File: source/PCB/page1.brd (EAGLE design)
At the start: 74.9 x 45.5 mm, 22 parts, among them J1 MJ88-BX11-RVSL2, J2 CONNECTOR-HEADER-6P-3460650P1, J4 CONNECTOR-HEADER-3P-3460810P1, J5 CONNECTOR-HEADER-2X3P-3460180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, Q3 MOSFET-N-044020001, Q4 MOSFET-N-044020001, U1 ATMEGA328P-AU-1030060P1, U2 A4988SETTR-QFN28

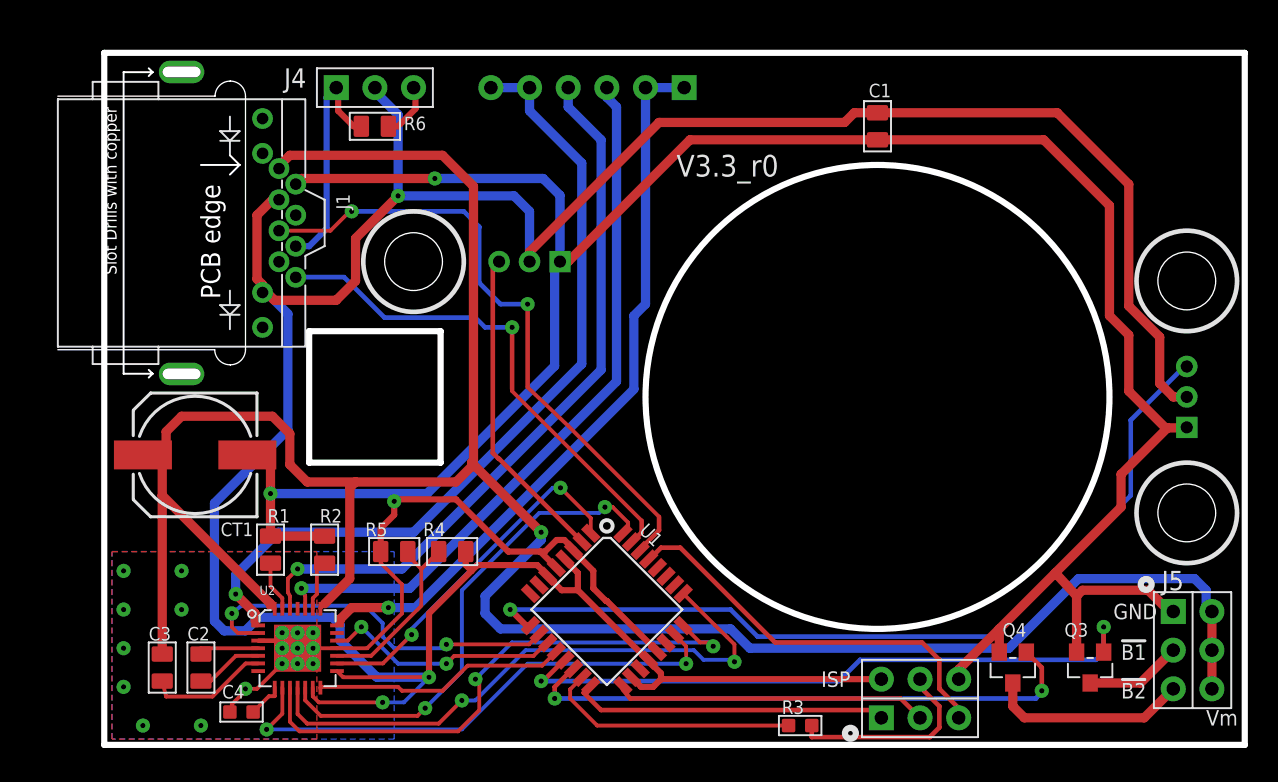
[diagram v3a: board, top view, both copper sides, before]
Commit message: updated pcb with better motor drivers -- tested and working.
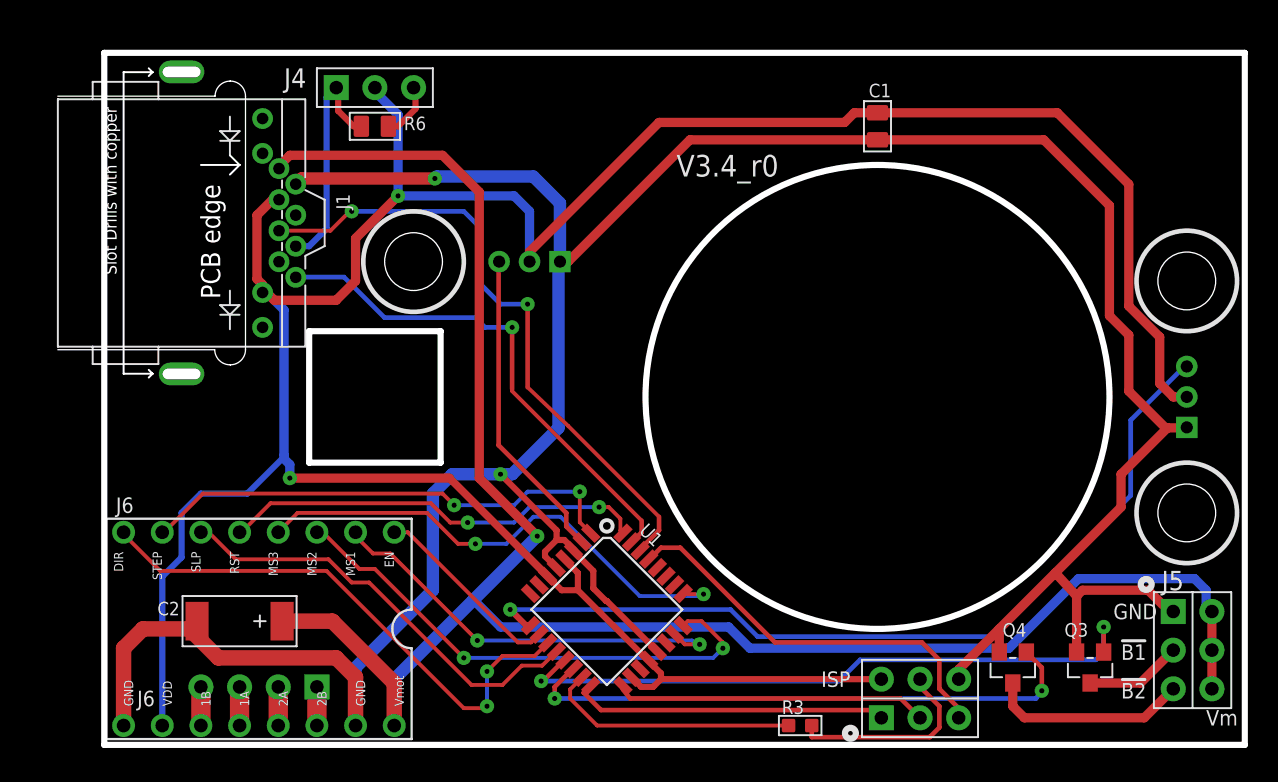
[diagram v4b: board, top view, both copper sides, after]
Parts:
- removed C3: 100nf, Seeed-OPL-Capacitor:C0805
- removed C4: 220nf, Seeed-OPL-Capacitor:C0603
- removed CT1: 100uf, Seeed-OPL-Capacitor:ELECTRO-SMD-E-7.8MM
- removed J2: CONNECTOR-HEADER-6P-3460650P1, OPL Eagle Library:1X6P-2.54-2.54-11.6-3.0-BLACK-MALE
- removed R1, R2: 0.2R 1/3W, Seeed-OPL-Resistor:R0805
- removed R4: 22K, Seeed-OPL-Resistor:R0805
- removed R5: 2.7K, Seeed-OPL-Resistor:R0805
- removed U2: A4988SETTR-QFN28, Seeed-OPL-ic:QFN28G_0.5-5X5MM
- added J3: 4p-2.54, Seeed-Connector -2016:H4-2.54
- added U$1: A4988BREAKOUT, RepRapjr:A4988BREAKOUT
- C2: value 100nf -> 47uf; device Seeed-OPL-Capacitor:C0805 -> Seeed-Capacitor-2016:AVX-C
- moved C2 3.97 mm to (8.89, 8.13)
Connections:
- removed net GND: C1.1, C4.1, CT1.-, ISP.4, J1.7, J5.1, Q3.2, Q4.2, R1.2, R2.2, R5.1, U$5.P$1, U$6.P$1, U1.21, U1.3, U1.5, U2.18, U2.29, U2.3
- removed net M1A: J2.3, U2.24
- removed net M1B: J2.1, J2.2, U2.21
- removed net M2A: J2.4, U2.26
- removed net M2B: J2.5, J2.6, U2.1
- removed net N$10: R4.1, R5.2, U2.17
- removed net N$2: R2.1, U2.23
- removed net N$5: R1.1, U2.27
- removed net N$6: C4.2, U2.8
- removed net N$7: C2.1, U2.5
- removed net N$8: C2.2, U2.4
- removed net N$9: C3.1, U2.6
- new net EEE: C1.1, C2.-, ISP.4, J1.7, J5.1, Q3.2, Q4.2, U$1.GND, U$1.GND@0, U$5.P$1, U$6.P$1, U1.21, U1.3, U1.5
- new net N$13: J3.1, U$1.2B
- new net N$14: J3.2, U$1.2A
- new net N$15: J3.3, U$1.1A
- new net N$16: J3.4, U$1.1B
- net +12V: now also C2.+, U$1.VMOT; no longer C3.2, CT1.+, U2.22, U2.28
- net +5V: now also U$1.VDD; no longer R4.2, U2.13, U2.15
- net M!EN: now also U$1.EN; no longer U2.2
- net M!RST: now also U$1.RST; no longer U2.12
- net M!SLP: now also U$1.SLP; no longer U2.14
- net MDIR: now also U$1.DIR; no longer U2.19
- net MS1: now also U$1.MS1; no longer U2.9
- net MS2: now also U$1.MS2; no longer U2.10
- net MS3: now also U$1.MS3; no longer U2.11
- net OC2B: now also U$1.STEP; no longer U2.16
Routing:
- net GND: track 215.5 -> 0.00 mm, vias 21 -> 0
- net EEE: track 0.00 -> 200.7 mm, vias 0 -> 2
- net M2B: track 54.6 -> 0.00 mm, vias 1 -> 0
- net M1B: track 48.7 -> 0.00 mm, vias 1 -> 0
- net M2A: track 47.7 -> 0.00 mm, vias 1 -> 0
- net M1A: track 47.3 -> 0.00 mm, vias 1 -> 0
- net +12V: track 164.3 -> 125.3 mm
- net MDIR: track 15.8 -> 35.8 mm
- net +5V: track 204.2 -> 188.0 mm, vias 3 -> 2
- net M!EN: track 25.2 -> 12.8 mm, vias 2 -> 0
- net N$10: track 12.4 -> 0.00 mm
- net M!SLP: track 16.8 -> 28.4 mm
- net OC2B: track 23.5 -> 32.2 mm
- net N$9: track 7.99 -> 0.00 mm
- net MS1: track 34.8 -> 27.7 mm
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- removed copper zone on layer 1, net GND
- removed copper zone on layer 16, net GND
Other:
- board text added: "J6"
- board text added: "V3.4_r0"
- board text removed: "V3.3_r0"
